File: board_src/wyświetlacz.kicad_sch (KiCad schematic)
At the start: 3 parts, among them J3 Conn_01x06

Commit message: wersja dodane arkusze hierarchiczne
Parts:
- R1: value 10 -> 100
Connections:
- net 3,3V renamed +3.3V
- net gnd renamed GND
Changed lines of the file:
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@@
+	(wire
+		(pts
+			(xy 125.73 119.38) (xy 125.73 124.46)
+		)
+		(stroke
+			(width 0)
+			(type default)
+		)
+	)
 	(wire
 		(pts
@@
 	(wire
 		(pts
-			(xy 119.38 60.96) (xy 119.38 63.5)
+			(xy 119.38 57.15) (xy 119.38 63.5)
 		)
 		(stroke
@@
 	(wire
 		(pts
-			(xy 121.92 60.96) (xy 119.38 60.96)
-		)
-		(stroke
-			(width 0)
-			(type default)
-		)
-	)
-	(wire
-		(pts
 			(xy 119.38 63.5) (xy 119.38 66.04)
 		)
@@
 			(width 0)
 			(type default)
-		)
-	)
-	(global_label "3,3V"
-		(shape input)
-		(at 121.92 60.96 0)
-		(fields_autoplaced yes)
-		(effects
-			(font
-				(size 1.27 1.27)
-			)
-			(justify left)
-		)
-		(property "Intersheetrefs" "${INTERSHEET_REFS}"
-			(at 129.0176 60.96 0)
-			(effects
-				(font
-					(size 1.27 1.27)
-				)
-				(justify left)
-				(hide yes)
-			)
-		)
-	)
-	(global_label "gnd"
-		(shape input)
-		(at 125.73 119.38 0)
-		(fields_autoplaced yes)
-		(effects
-			(font
-				(size 1.27 1.27)
-			)
-			(justify left)
-		)
-		(property "Intersheetrefs" "${INTERSHEET_REFS}"
-			(at 132.1622 119.38 0)
-			(effects
-				(font
-					(size 1.27 1.27)
-				)
-				(justify left)
-				(hide yes)
-			)
 		)
 	)
@@
 			)
 		)
-		(property "Value" "10"
+		(property "Value" "100"
 			(at 91.44 83.8199 0)
 			(effects
@@
 				(path "/772e9f49-cfcf-4cf6-843d-0684684f2d4b/13e729e2-af22-4566-902c-35554dc60200"
 					(reference "R1")
+					(unit 1)
+				)
+			)
+		)
+	)
+	(symbol
+		(lib_id "power:+3.3V")
+		(at 119.38 57.15 0)
+		(unit 1)
+		(exclude_from_sim no)
+		(in_bom yes)
+		(on_board yes)
+		(dnp no)
+		(fields_autoplaced yes)
+		(property "Reference" "#PWR09"
+			(at 119.38 60.96 0)
+			(effects
+				(font
+					(size 1.27 1.27)
+				)
+				(hide yes)
+			)
+		)
+		(property "Value" "+3.3V"
+			(at 119.38 52.07 0)
+			(effects
+				(font
+					(size 1.27 1.27)
+				)
+			)
+		)
+		(property "Footprint" ""
+			(at 119.38 57.15 0)
+			(effects
+				(font
+					(size 1.27 1.27)
+				)
+				(hide yes)
+			)
+		)
+		(property "Datasheet" ""
+			(at 119.38 57.15 0)
+			(effects
+				(font
+					(size 1.27 1.27)
+				)
+				(hide yes)
+			)
+		)
+		(property "Description" "Power symbol creates a global label with name \"+3.3V\""
+			(at 119.38 57.15 0)
+			(effects
+				(font
+					(size 1.27 1.27)
+				)
+				(hide yes)
+			)
+		)
+		(pin "1"
+		)
+		(instances
+			(project "board"
+				(path "/772e9f49-cfcf-4cf6-843d-0684684f2d4b/13e729e2-af22-4566-902c-35554dc60200"
+					(reference "#PWR09")
 					(unit 1)
 				)
@@
 					(unit 1)
 				)
+			)
+		)
+	)
+	(symbol
+		(lib_id "power:GND")
+		(at 125.73 124.46 0)
+		(unit 1)
+		(exclude_from_sim no)
+		(in_bom yes)
+		(on_board yes)
+		(dnp no)
+		(fields_autoplaced yes)
+		(property "Reference" "#PWR02"
+			(at 125.73 130.81 0)
+			(effects
+				(font
+					(size 1.27 1.27)
+				)
+				(hide yes)
+			)
+		)
+		(property "Value" "GND"
+			(at 125.73 129.54 0)
+			(effects
+				(font
+					(size 1.27 1.27)
+				)
+			)
+		)
+		(property "Footprint" ""
+			(at 125.73 124.46 0)
+			(effects
+				(font
+					(size 1.27 1.27)
+				)
+				(hide yes)
+			)
+		)
+		(property "Datasheet" ""
+			(at 125.73 124.46 0)
+			(effects
+				(font
+					(size 1.27 1.27)
+				)
+				(hide yes)
+			)
+		)
+		(property "Description" "Power symbol creates a global label with name \"GND\" , ground"
+			(at 125.73 124.46 0)
+			(effects
+				(font
+					(size 1.27 1.27)
+				)
+				(hide yes)
+			)
+		)
+		(pin "1"
+		)
+		(instances
+			(project ""
+				(path "/772e9f49-cfcf-4cf6-843d-0684684f2d4b/13e729e2-af22-4566-902c-35554dc60200"
+					(reference "#PWR02")
+					(unit 1)
+				)

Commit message: wersja dodane arkusze hierarchiczne
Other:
- moved on the sheet: R1
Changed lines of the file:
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@@
+	(wire
+		(pts
+			(xy 90.17 78.74) (xy 90.17 86.36)
+		)
+		(stroke
+			(width 0)
+			(type default)
+		)
+	)
 	(wire
 		(pts
@@
 	(wire
 		(pts
-			(xy 88.9 78.74) (xy 88.9 63.5)
+			(xy 90.17 71.12) (xy 90.17 63.5)
+		)
+		(stroke
+			(width 0)
+			(type default)
+		)
+	)
+	(wire
+		(pts
+			(xy 90.17 86.36) (xy 107.95 86.36)
 		)
 		(stroke
@@
 	(wire
 		(pts
-			(xy 88.9 63.5) (xy 119.38 63.5)
+			(xy 90.17 63.5) (xy 119.38 63.5)
 		)
 		(stroke
@@
 		(pts
 			(xy 119.38 119.38) (xy 125.73 119.38)
-		)
-		(stroke
-			(width 0)
-			(type default)
-		)
-	)
-	(wire
-		(pts
-			(xy 107.95 86.36) (xy 88.9 86.36)
 		)
 		(stroke
@@
 	(symbol
 		(lib_id "Device:R")
-		(at 88.9 82.55 0)
+		(at 90.17 74.93 0)
 		(unit 1)
 		(exclude_from_sim no)
@@
 		(fields_autoplaced yes)
 		(property "Reference" "R1"
-			(at 91.44 81.2799 0)
+			(at 92.71 73.6599 0)
 			(effects
 				(font
@@
 		)
 		(property "Value" "100"
-			(at 91.44 83.8199 0)
+			(at 92.71 76.1999 0)
 			(effects
 				(font
@@
 		)
 		(property "Footprint" ""
-			(at 87.122 82.55 90)
+			(at 88.392 74.93 90)
 			(effects
 				(font
@@
 		)
 		(property "Datasheet" "~"
-			(at 88.9 82.55 0)
+			(at 90.17 74.93 0)
 			(effects
 				(font
@@
 		)
 		(property "Description" "Resistor"
-			(at 88.9 82.55 0)
-			(effects
-				(font
+			(at 90.17 74.93 0)
+			(effects
+				(font

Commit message: wersja z przetwornikiem
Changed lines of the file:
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@@
 	(paper "A4")
 	(junction
+		(at 119.38 60.96)
+		(diameter 0)
+		(color 0 0 0 0)
+	)
+	(junction
 		(at 97.79 91.44)
 		(diameter 0)
@@
 	)
 	(junction
+		(at 124.46 119.38)
+		(diameter 0)
+		(color 0 0 0 0)
+	)
+	(junction
 		(at 119.38 63.5)
 		(diameter 0)
@@
 	(wire
 		(pts
+			(xy 124.46 116.84) (xy 124.46 119.38)
+		)
+		(stroke
+			(width 0)
+			(type default)
+		)
+	)
+	(wire
+		(pts
 			(xy 97.79 91.44) (xy 107.95 91.44)
 		)
@@
 	(wire
 		(pts
-			(xy 119.38 57.15) (xy 119.38 63.5)
+			(xy 119.38 57.15) (xy 119.38 60.96)
 		)
 		(stroke
@@
 	(wire
 		(pts
+			(xy 123.19 60.96) (xy 119.38 60.96)
+		)
+		(stroke
+			(width 0)
+			(type default)
+		)
+	)
+	(wire
+		(pts
 			(xy 90.17 86.36) (xy 107.95 86.36)
 		)
@@
 	(wire
 		(pts
+			(xy 119.38 60.96) (xy 119.38 63.5)
+		)
+		(stroke
+			(width 0)
+			(type default)
+		)
+	)
+	(wire
+		(pts
 			(xy 119.38 63.5) (xy 119.38 66.04)
 		)
@@
 	(wire
 		(pts
-			(xy 119.38 119.38) (xy 125.73 119.38)
+			(xy 123.19 58.42) (xy 123.19 60.96)
+		)
+		(stroke
+			(width 0)
+			(type default)
+		)
+	)
+	(wire
+		(pts
+			(xy 119.38 119.38) (xy 124.46 119.38)
+		)
+		(stroke
+			(width 0)
+			(type default)
+		)
+	)
+	(wire
+		(pts
+			(xy 124.46 119.38) (xy 125.73 119.38)
 		)
 		(stroke
@@
 			(width 0)
 			(type default)
+		)
+	)
+	(symbol
+		(lib_id "power:PWR_FLAG")
+		(at 123.19 58.42 0)
+		(unit 1)
+		(exclude_from_sim no)
+		(in_bom yes)
+		(on_board yes)
+		(dnp no)
+		(property "Reference" "#FLG07"
+			(at 123.19 56.515 0)
+			(effects
+				(font
+					(size 1.27 1.27)
+				)
+				(hide yes)
+			)
+		)
+		(property "Value" "PWR_FLAG"
+			(at 130.048 56.642 0)
+			(effects
+				(font
+					(size 1.27 1.27)
+				)
+			)
+		)
+		(property "Footprint" ""
+			(at 123.19 58.42 0)
+			(effects
+				(font
+					(size 1.27 1.27)
+				)
+				(hide yes)
+			)
+		)
+		(property "Datasheet" "~"
+			(at 123.19 58.42 0)
+			(effects
+				(font
+					(size 1.27 1.27)
+				)
+				(hide yes)
+			)
+		)
+		(property "Description" "Special symbol for telling ERC where power comes from"
+			(at 123.19 58.42 0)
+			(effects
+				(font
+					(size 1.27 1.27)
+				)
+				(hide yes)
+			)
+		)
+		(pin "1"
+		)
+		(instances
+			(project "board"
+				(path "/772e9f49-cfcf-4cf6-843d-0684684f2d4b/13e729e2-af22-4566-902c-35554dc60200"
+					(reference "#FLG07")
+					(unit 1)
+				)
+			)
 		)
 	)
@@
 					(unit 1)
 				)
+			)
+		)
+	)
+	(symbol
+		(lib_id "power:PWR_FLAG")
+		(at 124.46 116.84 0)
+		(unit 1)
+		(exclude_from_sim no)
+		(in_bom yes)
+		(on_board yes)
+		(dnp no)
+		(property "Reference" "#FLG06"
+			(at 124.46 114.935 0)
+			(effects
+				(font
+					(size 1.27 1.27)
+				)
+				(hide yes)
+			)
+		)
+		(property "Value" "PWR_FLAG"
+			(at 131.318 115.062 0)
+			(effects
+				(font
+					(size 1.27 1.27)
+				)
+			)
+		)
+		(property "Footprint" ""
+			(at 124.46 116.84 0)
+			(effects
+				(font
+					(size 1.27 1.27)
+				)
+				(hide yes)
+			)
+		)
+		(property "Datasheet" "~"
+			(at 124.46 116.84 0)
+			(effects
+				(font
+					(size 1.27 1.27)
+				)
+				(hide yes)
+			)
+		)
+		(property "Description" "Special symbol for telling ERC where power comes from"
+			(at 124.46 116.84 0)
+			(effects
+				(font
+					(size 1.27 1.27)
+				)
+				(hide yes)
+			)
+		)
+		(pin "1"
+		)
+		(instances
+			(project "board"
+				(path "/772e9f49-cfcf-4cf6-843d-0684684f2d4b/13e729e2-af22-4566-902c-35554dc60200"
+					(reference "#FLG06")
+					(unit 1)
+				)

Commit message: wersja uzupelnione footprinty
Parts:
- J3: footprint (none) -> Connector_PinHeader_2.54mm:PinHeader_1x06_P2.54mm_Vertical
- R1: footprint (none) -> Resistor_SMD:R_0201_0603Metric
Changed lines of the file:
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@@
 			)
 		)
-		(property "Footprint" ""
+		(property "Footprint" "Resistor_SMD:R_0201_0603Metric"
 			(at 88.392 74.93 90)
 			(effects
@@
 			)
 		)
-		(property "Footprint" ""
+		(property "Footprint" "Connector_PinHeader_2.54mm:PinHeader_1x06_P2.54mm_Vertical"
 			(at 97.79 78.74 0)
 			(effects

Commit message: wersja z FT232RN
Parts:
- R1: footprint Resistor_SMD:R_0201_0603Metric -> Resistor_SMD:R_1206_3216Metric
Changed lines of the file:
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@@
 			)
 		)
-		(property "Footprint" "Resistor_SMD:R_0201_0603Metric"
+		(property "Footprint" "Resistor_SMD:R_1206_3216Metric"
 			(at 88.392 74.93 90)
 			(effects

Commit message: Wersja ze sciezkami miedzianymi
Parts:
- R1: footprint Resistor_SMD:R_1206_3216Metric -> Resistor_SMD:R_0603_1608Metric
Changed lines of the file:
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@@
 			)
 		)
-		(property "Footprint" "Resistor_SMD:R_1206_3216Metric"
+		(property "Footprint" "Resistor_SMD:R_0603_1608Metric"
 			(at 88.392 74.93 90)
 			(effects

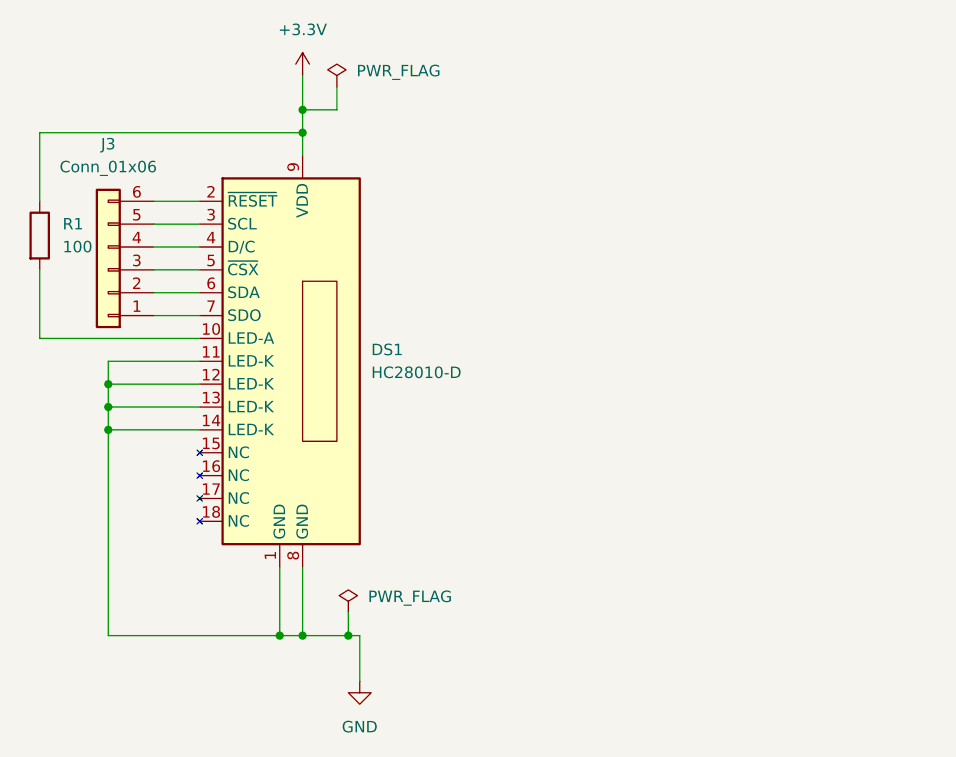
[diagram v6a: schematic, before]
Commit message: dodany tranzystor BS123
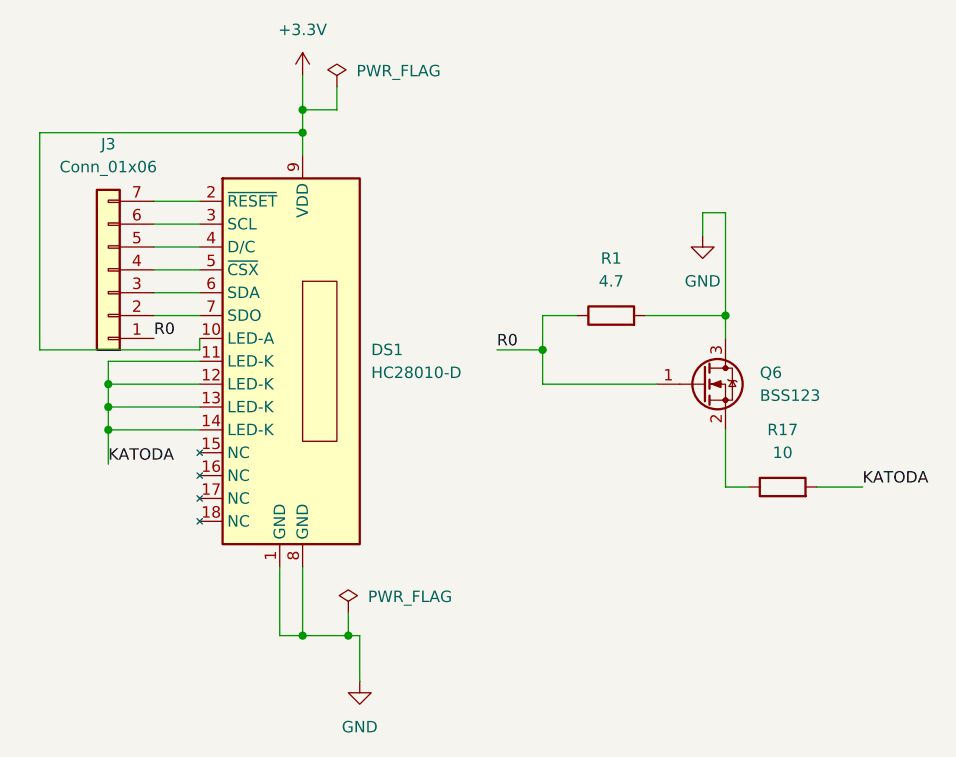
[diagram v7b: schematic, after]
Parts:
- added Q6: BSS123, Package_TO_SOT_SMD:SOT-23, symbol Transistor_FET:BSS123
- added R17: 10, Resistor_SMD:R_0603_1608Metric, symbol Device:R
- J3: footprint Connector_PinHeader_2.54mm:PinHeader_1x06_P2.54mm_Vertical -> Connector_PinHeader_2.54mm:PinHeader_1x07_P2.54mm_Vertical; symbol Connector_Generic:Conn_01x06 -> Connector_Generic:Conn_01x07
- R1: value 100 -> 4.7
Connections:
- net +3.3V: now also DS1.10 (LED-A); no longer R1.1
- net GND: now also R1.2, Q6.3 (D); no longer DS1.11 (LED-K), DS1.12 (LED-K), DS1.13 (LED-K), DS1.14 (LED-K)
- net at DS1.2 (~{RESET}): now also J3.7 (Pin_7); no longer J3.6 (Pin_6)
- net at DS1.3 (SCL): now also J3.6 (Pin_6); no longer J3.5 (Pin_5)
- net at DS1.4 (D/C): now also J3.5 (Pin_5); no longer J3.4 (Pin_4)
- net at DS1.5 (~{CSX}): now also J3.4 (Pin_4); no longer J3.3 (Pin_3)
- net at DS1.6 (SDA): now also J3.3 (Pin_3); no longer J3.2 (Pin_2)
- net at DS1.7 (SDO): now also J3.2 (Pin_2); no longer J3.1 (Pin_1)
- new net: Q6.2 (S), R17.1
- new net KATODA: DS1.11 (LED-K), DS1.12 (LED-K), DS1.13 (LED-K), DS1.14 (LED-K), R17.2
- new net R0: J3.1 (Pin_1), Q6.1 (G), R1.1

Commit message: finalna wersja, naniesione poprawki
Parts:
- R1: value 4.7 -> 4.7k
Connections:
- net GND: now also Q6.2 (S); no longer Q6.3 (D)
- net at R17.1: now also Q6.3 (D); no longer Q6.2 (S)
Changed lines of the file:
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@@
 		(lib_id "Transistor_FET:BSS123")
 		(at 163.83 91.44 0)
-		(unit 1)
-		(exclude_from_sim no)
-		(in_bom yes)
-		(on_board yes)
-		(dnp no)
-		(fields_autoplaced yes)
+		(mirror x)
+		(unit 1)
+		(exclude_from_sim no)
+		(in_bom yes)
+		(on_board yes)
+		(dnp no)
 		(property "Reference" "Q6"
-			(at 170.18 90.1699 0)
+			(at 170.18 92.7101 0)
 			(effects
 				(font
@@
 		)
 		(property "Value" "BSS123"
-			(at 170.18 92.7099 0)
+			(at 170.18 90.1701 0)
 			(effects
 				(font
@@
 		)
 		(property "Footprint" "Package_TO_SOT_SMD:SOT-23"
-			(at 168.91 93.345 0)
+			(at 168.91 89.535 0)
 			(effects
 				(font
@@
 		)
 		(property "Datasheet" "http://www.diodes.com/assets/Datasheets/ds30366.pdf"
-			(at 168.91 95.25 0)
+			(at 168.91 87.63 0)
 			(effects
 				(font
@@
 			)
 		)
-		(property "Value" "4.7"
+		(property "Value" "4.7k"
 			(at 153.67 80.01 90)
 			(effects
